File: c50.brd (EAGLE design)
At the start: 93.7 x 31.7 mm, 15 parts, among them IC1 7805TV, IC2 UA555N

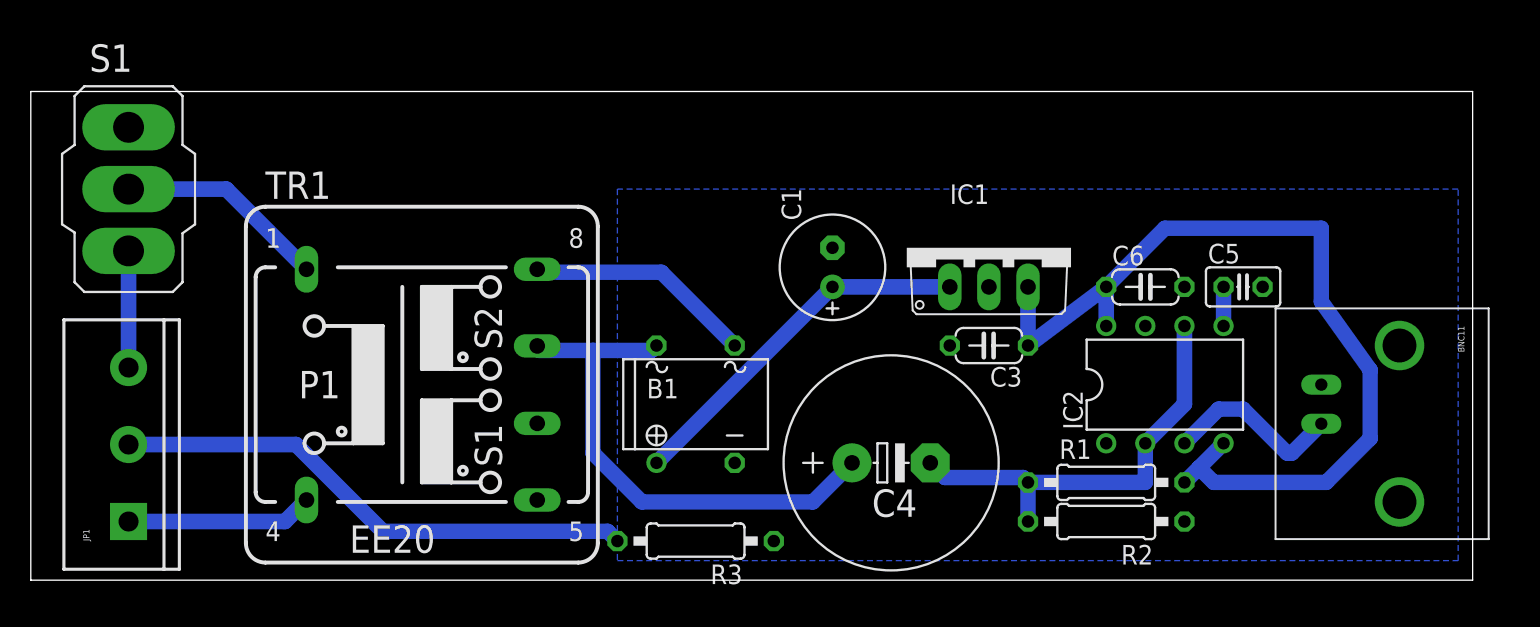
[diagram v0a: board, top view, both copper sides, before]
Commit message: Update to final design. Send gerber files to the workshop.
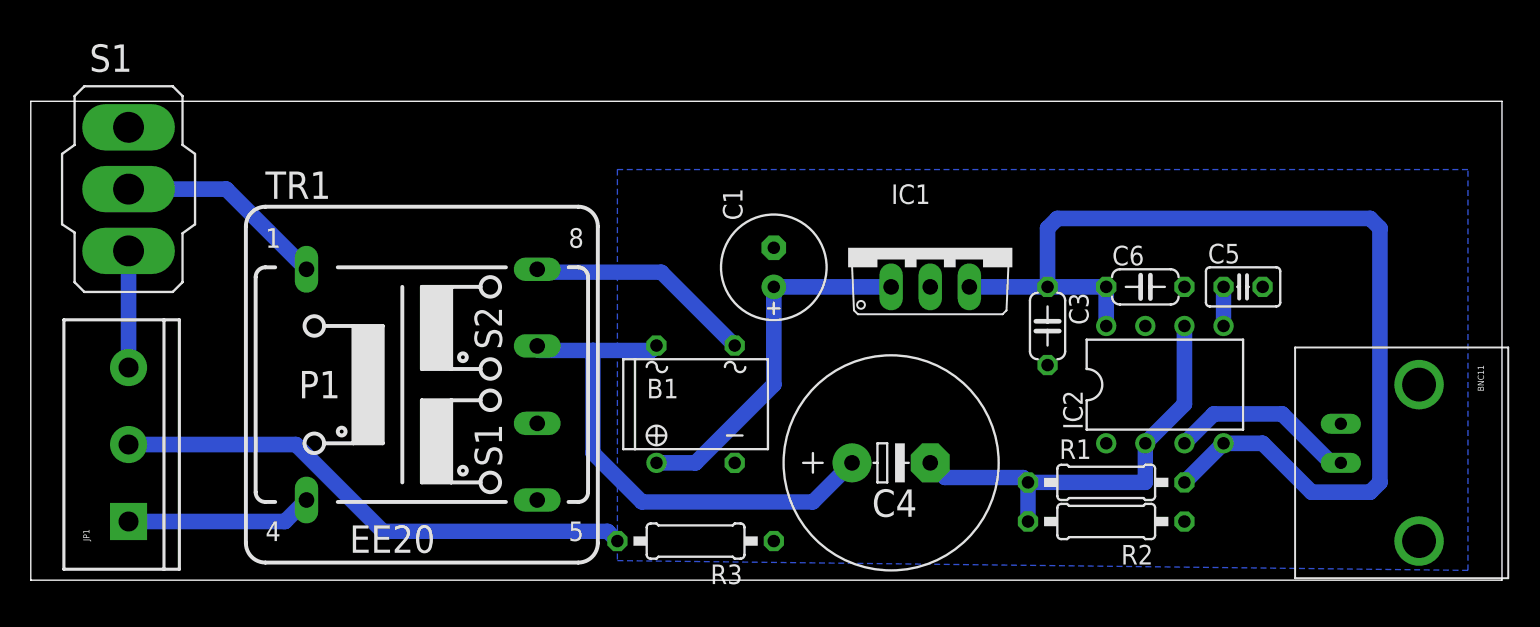
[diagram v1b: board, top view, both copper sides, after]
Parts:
- moved C3 4.02 mm to (66.0, 16.5), turned to 270 degrees
- moved C1 3.81 mm to (48.3, 20.3)
- moved IC1 3.81 mm to (58.4, 21.6)
- moved BNC11 2.84 mm to (85.1, 7.62)
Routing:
- net V+: track 59.2 -> 69.2 mm
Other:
- board size 93.7 x 31.7 mm -> 95.6 x 31.1 mm
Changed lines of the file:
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@@
 <setting verticaltext="up"/>
 </settings>
-<grid distance="0.05" unitdist="inch" unit="inch" style="lines" multiple="1" display="yes" altdistance="0.025" altunitdist="inch" altunit="inch"/>
+<grid distance="0.05" unitdist="inch" unit="inch" style="lines" multiple="1" display="yes" altdistance="0.0125" altunitdist="inch" altunit="inch"/>
 <layers>
 <layer number="1" name="Top" color="4" fill="1" visible="yes" active="yes"/>
@@
 <layer number="43" name="vRestrict" color="2" fill="10" visible="yes" active="yes"/>
 <layer number="44" name="Drills" color="7" fill="1" visible="no" active="yes"/>
-<layer number="45" name="Holes" color="7" fill="1" visible="no" active="yes"/>
+<layer number="45" name="Holes" color="7" fill="1" visible="yes" active="yes"/>
 <layer number="46" name="Milling" color="3" fill="1" visible="no" active="yes"/>
 <layer number="47" name="Measures" color="7" fill="1" visible="no" active="yes"/>
@@
 <board>
 <plain>
-<wire x1="0" y1="0" x2="93.65" y2="0" width="0" layer="20"/>
-<wire x1="93.65" y1="0" x2="93.65" y2="31.74" width="0" layer="20"/>
-<wire x1="93.65" y1="31.74" x2="0" y2="31.74" width="0" layer="20"/>
-<wire x1="0" y1="31.74" x2="0" y2="0" width="0" layer="20"/>
-<dimension x1="0" y1="25.39" x2="0" y2="0" x3="-3.81" y3="12.695" textsize="1.778" layer="20"/>
-<dimension x1="0" y1="0" x2="93.65" y2="0" x3="46.825" y3="-5.08" textsize="1.778" layer="20"/>
+<wire x1="0" y1="0" x2="95.555" y2="0" width="0" layer="20"/>
+<wire x1="95.555" y1="0" x2="95.555" y2="31.105" width="0" layer="20"/>
+<wire x1="95.555" y1="31.105" x2="0" y2="31.105" width="0" layer="20"/>
+<wire x1="0" y1="31.105" x2="0" y2="0" width="0" layer="20"/>
+<dimension x1="0" y1="0" x2="0" y2="31.105" x3="-4.445" y3="15.5525" textsize="1.778" layer="20"/>
+<dimension x1="0" y1="0" x2="95.555" y2="0" x3="47.7775" y3="-5.08" textsize="1.778" layer="20"/>
 </plain>
 <attributes>
@@
 <attribute name="VALUE" x="53.848" y="1.143" size="1.778" layer="27" ratio="10"/>
 </element>
-<element name="C3" library="resistor" package="C050-024X044" value="100n" x="62.23" y="15.24" rot="R180"/>
-<element name="C1" library="rcl" package="E2,5-7" value="100u" x="52.07" y="20.32" rot="R90"/>
+<element name="C3" library="resistor" package="C050-024X044" value="100n" x="66.04" y="16.51" rot="R270"/>
+<element name="C1" library="rcl" package="E2,5-7" value="100u" x="48.26" y="20.32" rot="R90"/>
 <element name="C5" library="rcl" package="C025-025X050" value="10n" x="78.74" y="19.05"/>
 <element name="IC2" library="linear" package="DIL08" value="UA555N" x="73.66" y="12.7"/>
-<element name="IC1" library="linear" package="TO220V" value="7805TV" x="62.23" y="21.59" smashed="yes">
-<attribute name="NAME" x="59.69" y="24.4348" size="1.27" layer="25" ratio="10"/>
-<attribute name="VALUE" x="59.69" y="22.86" size="1.27" layer="27" ratio="10"/>
+<element name="IC1" library="linear" package="TO220V" value="7805TV" x="58.42" y="21.59" smashed="yes">
+<attribute name="NAME" x="55.88" y="24.4348" size="1.27" layer="25" ratio="10"/>
+<attribute name="VALUE" x="55.88" y="22.86" size="1.27" layer="27" ratio="10"/>
 </element>
 <element name="R2" library="resistor" package="0207/10" value="1k" x="69.85" y="3.81" rot="R180"/>
@@
 <element name="TR1" library="trafo" package="EE20-2" value="230-6V" x="25.4" y="12.7"/>
 <element name="C6" library="resistor" package="C050-024X044" value="100n" x="72.39" y="19.05"/>
-<element name="BNC11" library="SparkFun-Connectors" package="BNC" value="BNCPTH" x="83.82" y="10.16" rot="R270"/>
+<element name="BNC11" library="SparkFun-Connectors" package="BNC" value="BNCPTH" x="85.09" y="7.62" rot="R270"/>
 <element name="R3" library="resistor" package="0207/10" value="220k" x="43.18" y="2.54" rot="R180"/>
 <element name="JP1" library="SparkFun-Connectors" package="SCREWTERMINAL-5MM-3" value="mains" x="6.35" y="3.81" rot="R90">
@@
 <contactref element="R3" pad="1"/>
 <polygon width="0.4064" layer="16">
-<vertex x="38.1" y="25.4"/>
+<vertex x="38.1" y="26.67"/>
 <vertex x="38.1" y="1.27"/>
-<vertex x="92.71" y="1.27"/>
-<vertex x="92.71" y="25.4"/>
+<vertex x="93.345" y="0.635"/>
+<vertex x="93.345" y="26.67"/>
 </polygon>
 </signal>
@@
 <contactref element="C1" pad="+"/>
 <contactref element="IC1" pad="1"/>
-<wire x1="59.69" y1="19.05" x2="52.07" y2="19.05" width="1.016" layer="16"/>
-<wire x1="52.07" y1="19.05" x2="40.64" y2="7.62" width="1.016" layer="16"/>
+<wire x1="55.88" y1="19.05" x2="48.26" y2="19.05" width="1.016" layer="16"/>
+<wire x1="40.64" y1="7.62" x2="43.18" y2="7.62" width="1.016" layer="16"/>
+<wire x1="43.18" y1="7.62" x2="48.26" y2="12.7" width="1.016" layer="16"/>
+<wire x1="48.26" y1="19.05" x2="48.26" y2="12.7" width="1.016" layer="16"/>
 </signal>
 <signal name="V+">
@@
 <contactref element="IC2" pad="8"/>
 <contactref element="C6" pad="1"/>
-<wire x1="77.47" y1="8.89" x2="75.8825" y2="7.3025" width="1" layer="16"/>
-<wire x1="75.8825" y1="7.3025" x2="74.93" y2="6.35" width="1" layer="16"/>
-<wire x1="76.835" y1="6.35" x2="75.8825" y2="7.3025" width="1" layer="16"/>
-<wire x1="84.1375" y1="6.35" x2="76.835" y2="6.35" width="1" layer="16"/>
-<wire x1="86.995" y1="9.2075" x2="84.1375" y2="6.35" width="1" layer="16"/>
-<wire x1="86.995" y1="13.6525" x2="86.995" y2="9.2075" width="1" layer="16"/>
-<wire x1="83.82" y1="18.0975" x2="86.995" y2="13.6525" width="1" layer="16"/>
-<wire x1="83.82" y1="22.86" x2="83.82" y2="18.0975" width="1" layer="16"/>
-<wire x1="73.66" y1="22.86" x2="83.82" y2="22.86" width="1" layer="16"/>
-<wire x1="69.85" y1="19.05" x2="73.66" y2="22.86" width="1" layer="16"/>
 <wire x1="69.85" y1="16.51" x2="69.85" y2="19.05" width="1.016" layer="16"/>
-<wire x1="69.85" y1="19.05" x2="64.77" y2="15.24" width="1.016" layer="16"/>
-<wire x1="64.77" y1="19.05" x2="64.77" y2="15.24" width="1.016" layer="16"/>
+<wire x1="69.85" y1="19.05" x2="66.04" y2="19.05" width="1.016" layer="16"/>
+<wire x1="60.96" y1="19.05" x2="66.04" y2="19.05" width="1.016" layer="16"/>
+<wire x1="74.93" y1="6.35" x2="77.47" y2="8.89" width="1.016" layer="16"/>
+<wire x1="77.47" y1="8.89" x2="80.01" y2="8.89" width="1.016" layer="16"/>
+<wire x1="80.01" y1="8.89" x2="83.185" y2="5.715" width="1.016" layer="16"/>
+<wire x1="83.185" y1="5.715" x2="86.995" y2="5.715" width="1.016" layer="16"/>
+<wire x1="86.995" y1="5.715" x2="87.63" y2="6.35" width="1.016" layer="16"/>
+<wire x1="87.63" y1="6.35" x2="87.63" y2="22.86" width="1.016" layer="16"/>
+<wire x1="87.63" y1="22.86" x2="86.995" y2="23.495" width="1.016" layer="16"/>
+<wire x1="66.675" y1="23.495" x2="66.04" y2="22.86" width="1.016" layer="16"/>
+<wire x1="66.04" y1="22.86" x2="66.04" y2="19.05" width="1.016" layer="16"/>
+<wire x1="86.995" y1="23.495" x2="66.675" y2="23.495" width="1.016" layer="16"/>
 </signal>
 <signal name="N$7">
@@
 <contactref element="IC2" pad="3"/>
 <contactref element="BNC11" pad="S"/>
-<wire x1="81.915" y1="8.255" x2="83.82" y2="10.16" width="1" layer="16"/>
-<wire x1="81.5975" y1="8.255" x2="81.915" y2="8.255" width="1" layer="16"/>
-<wire x1="78.74" y1="11.1125" x2="81.5975" y2="8.255" width="1" layer="16"/>
-<wire x1="77.1525" y1="11.1125" x2="78.74" y2="11.1125" width="1" layer="16"/>
-<wire x1="74.93" y1="8.89" x2="77.1525" y2="11.1125" width="1" layer="16"/>
+<wire x1="74.93" y1="8.89" x2="76.835" y2="10.795" width="1.016" layer="16"/>
+<wire x1="85.09" y1="7.62" x2="84.455" y2="7.62" width="1.016" layer="16"/>
+<wire x1="84.455" y1="7.62" x2="81.28" y2="10.795" width="1.016" layer="16"/>
+<wire x1="81.28" y1="10.795" x2="76.835" y2="10.795" width="1.016" layer="16"/>
 </signal>
 <signal name="N$2">

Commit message: Signature added.
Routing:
- net N$11: track 0.00 -> 8.29 mm
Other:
- board text added: "- C50"
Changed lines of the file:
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@@
 <setting verticaltext="up"/>
 </settings>
-<grid distance="0.05" unitdist="inch" unit="inch" style="lines" multiple="1" display="yes" altdistance="0.0125" altunitdist="inch" altunit="inch"/>
+<grid distance="0.005" unitdist="inch" unit="inch" style="lines" multiple="1" display="yes" altdistance="0.0125" altunitdist="inch" altunit="inch"/>
 <layers>
 <layer number="1" name="Top" color="4" fill="1" visible="yes" active="yes"/>
@@
 <dimension x1="0" y1="0" x2="0" y2="31.105" x3="-4.445" y3="15.5525" textsize="1.778" layer="20"/>
 <dimension x1="0" y1="0" x2="95.555" y2="0" x3="47.7775" y3="-5.08" textsize="1.778" layer="20"/>
+<text x="90.678" y="27.305" size="1.778" layer="16" rot="MR0"> - C50</text>
 </plain>
 <attributes>
@@
 <contactref element="R3" pad="1"/>
 <polygon width="0.4064" layer="16">
-<vertex x="38.1" y="26.67"/>
+<vertex x="38.1" y="25.908"/>
 <vertex x="38.1" y="1.27"/>
 <vertex x="93.345" y="0.635"/>
-<vertex x="93.345" y="26.67"/>
+<vertex x="93.345" y="25.908"/>
 </polygon>
 </signal>
@@
 <wire x1="6.35" y1="13.81" x2="6.35" y2="21.3868" width="1.016" layer="16"/>
 </signal>
+<signal name="N$11">
+<wire x1="91.8845" y1="28.829" x2="92.456" y2="29.972" width="0.254" layer="16"/>
+<wire x1="92.456" y1="29.972" x2="93.218" y2="28.2575" width="0.254" layer="16"/>
+<wire x1="93.218" y1="28.2575" x2="92.456" y2="26.924" width="0.254" layer="16"/>
+<wire x1="92.456" y1="26.924" x2="91.8845" y2="27.8765" width="0.254" layer="16"/>
+<wire x1="91.8845" y1="27.8765" x2="91.5035" y2="27.305" width="0.254" layer="16"/>
+<wire x1="91.5035" y1="27.305" x2="91.1225" y2="27.8765" width="0.254" layer="16"/>
+<wire x1="91.1225" y1="27.8765" x2="90.551" y2="26.924" width="0.254" layer="16"/>
+</signal>
 </signals>

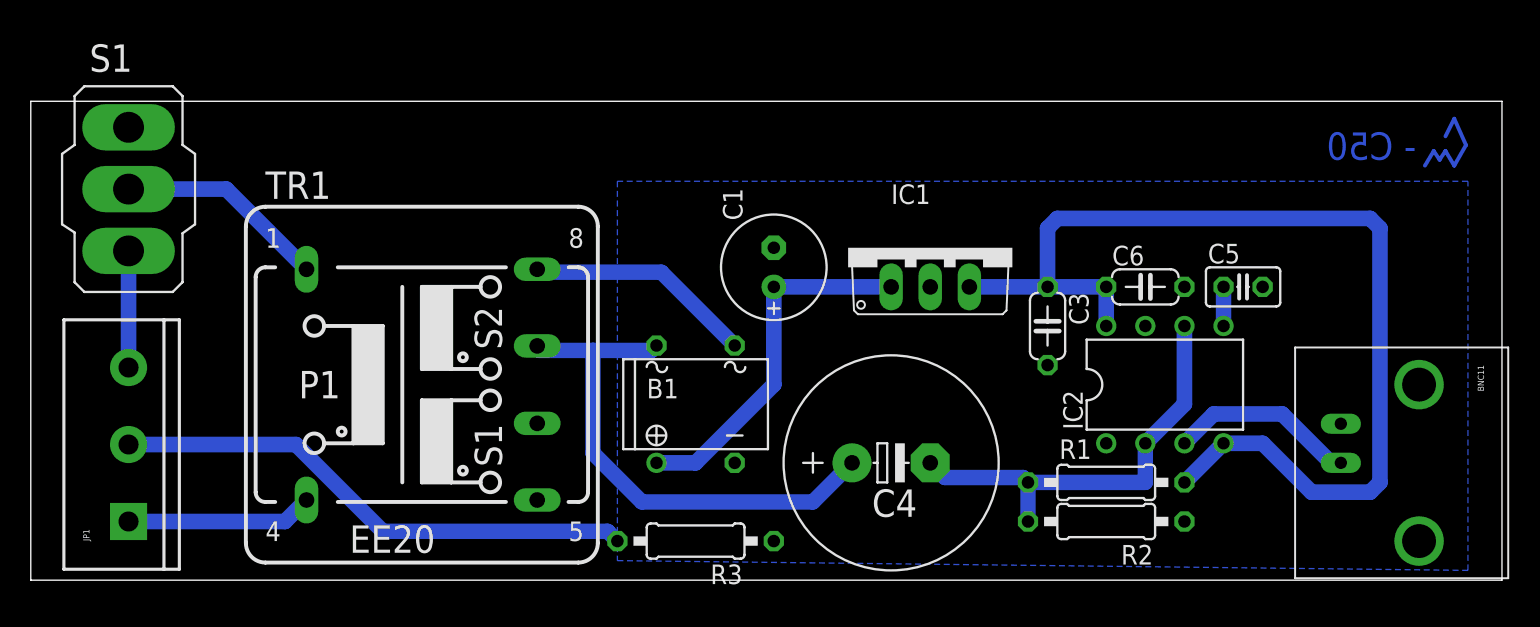
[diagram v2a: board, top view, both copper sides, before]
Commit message: Modified gerbers, sistemati drill e holes. Routing da finire.
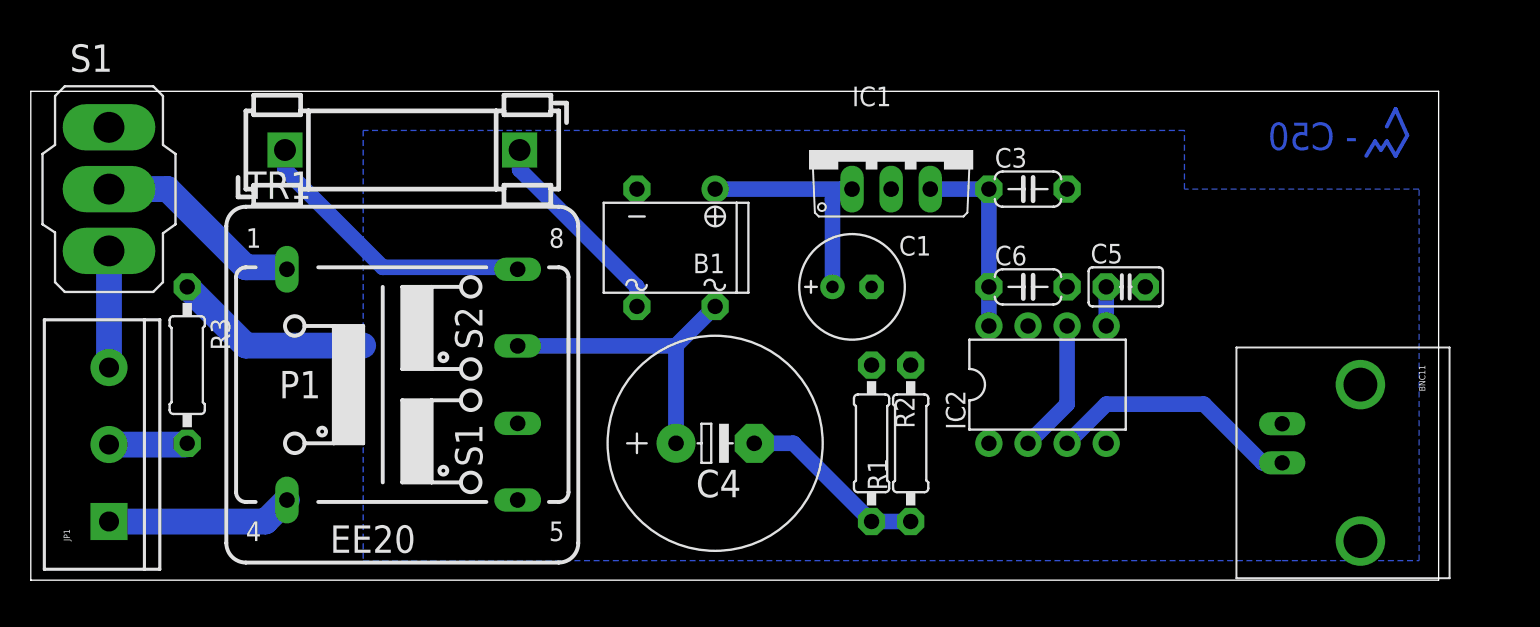
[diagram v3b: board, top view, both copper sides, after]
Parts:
- added F1: FUSEBLANK_5X20MM, fuse:FUSE_HOLDER_5X20MM
- moved R3 34.9 mm to (10.2, 14.0), turned to 270 degrees
- moved R2 16.1 mm to (54.6, 8.89), turned to 270 degrees
- moved R1 13.0 mm to (57.1, 8.89), turned to 90 degrees
- moved C4 11.5 mm to (44.5, 8.89)
- moved B1 10.2 mm to (41.9, 21.6), turned to 180 degrees
- moved C3 8.98 mm to (64.8, 25.4), turned to 0 degrees
- moved C6 7.62 mm to (64.8, 19.1)
- moved C5 7.62 mm to (71.1, 19.1)
- moved IC2 7.62 mm to (66.0, 12.7)
- moved IC1 6.84 mm to (55.9, 27.9)
- moved C1 5.24 mm to (53.3, 19.1), turned to 0 degrees
- moved BNC11 3.81 mm to (81.3, 7.62)
- moved JP1 1.27 mm to (5.08, 3.81)
- moved S1 1.27 mm to (5.08, 25.4)
- moved TR1 1.27 mm to (24.1, 12.7)
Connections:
- new net N$13: B1.AC1, F1.2
- net N$6: now also F1.1; no longer B1.AC1
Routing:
- net V+: track 69.2 -> 12.7 mm
- net N$4: track 34.3 -> 5.11 mm
- net N$2: track 33.9 -> 20.2 mm
- net N$13: track 0.00 -> 13.3 mm
- net GND: track 0.00 -> 13.0 mm
- net N$5: track 23.7 -> 16.1 mm
- net N$8: track 28.2 -> 20.9 mm
- net N$9: track 12.3 -> 16.6 mm
- net N$6: track 14.9 -> 19.1 mm
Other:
- board size 95.6 x 31.1 mm -> 91.4 x 31.8 mm

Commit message: Finished (maybe)
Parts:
- C5: device rcl:C025-025X050 -> resistor:C050-024X044
- moved C6 6.84 mm to (58.4, 16.5), turned to 180 degrees
- moved BNC11 6.35 mm to (74.9, 7.62)
- moved IC2 2.84 mm to (64.8, 10.2)
- moved C1 2.54 mm to (50.8, 19.1)
- moved C5 2.54 mm to (71.1, 16.5)
- moved IC1 2.54 mm to (53.3, 27.9)
- moved C3 1.27 mm to (63.5, 25.4)
- moved R1 1.27 mm to (55.9, 8.89)
- moved R2 1.27 mm to (53.3, 8.89)
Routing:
- net V+: track 12.7 -> 45.3 mm
- net N$8: track 20.9 -> 28.8 mm
- net N$9: track 16.6 -> 12.3 mm
- net N$5: track 16.1 -> 13.6 mm
- net GND: track 13.0 -> 15.5 mm
- added copper zone on layer 16, net N$12
- added copper zone on layer 16, net N$15
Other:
- board size 91.4 x 31.8 mm -> 85.1 x 31.8 mm
